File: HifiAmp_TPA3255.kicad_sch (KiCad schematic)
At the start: 129 parts, among them J1 PVDD 48V IN — NEEDS_DATA, J2 RCA L SE, J3 RCA R SE, J301 SPK_L, J302 SPK_R, J4 VOLUME_REMOTE, Q301 IPP330P10NM, Q302 IXTK200N10L2, U1 LM5010ASD, U2 LM2940IMP-12/NOPB, U3 TLV1117-33IDCY, U4 OPA1612AIDR, U5 OPA1612AIDR, U6 TPA3255B, U7 TPS3802K33DCKR, U8 LM5069-2

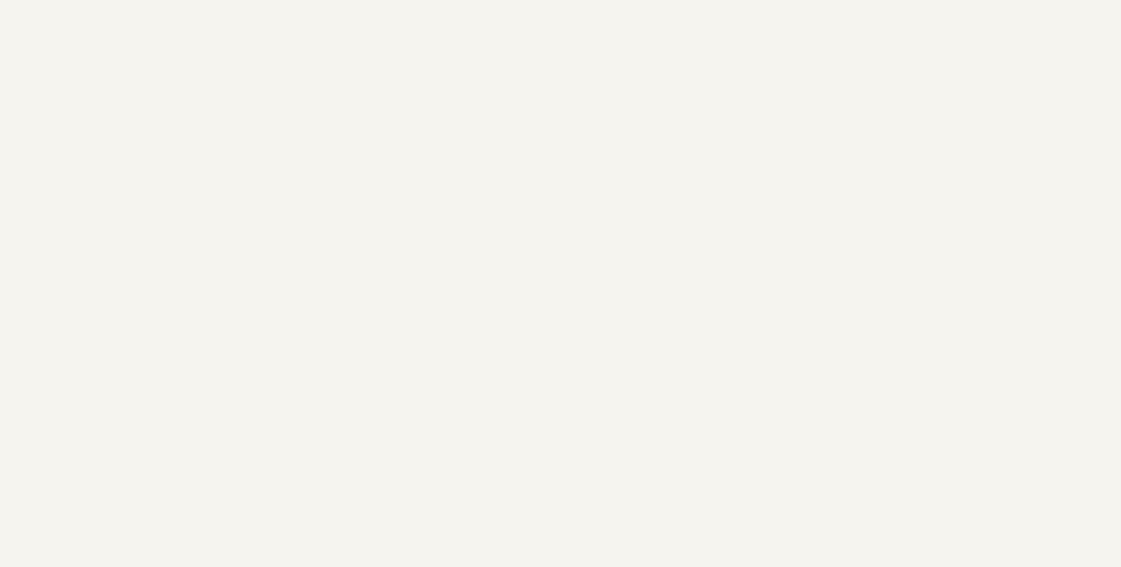
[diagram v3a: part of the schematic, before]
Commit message: feat(h1.4): add the TI Fig. 29 output RC networks (1 nF, 3.3 ohm + 10 nF) on OUT_A-D_F
Co-Authored-By: Claude Opus 5.5 <noreply@anthropic.com>
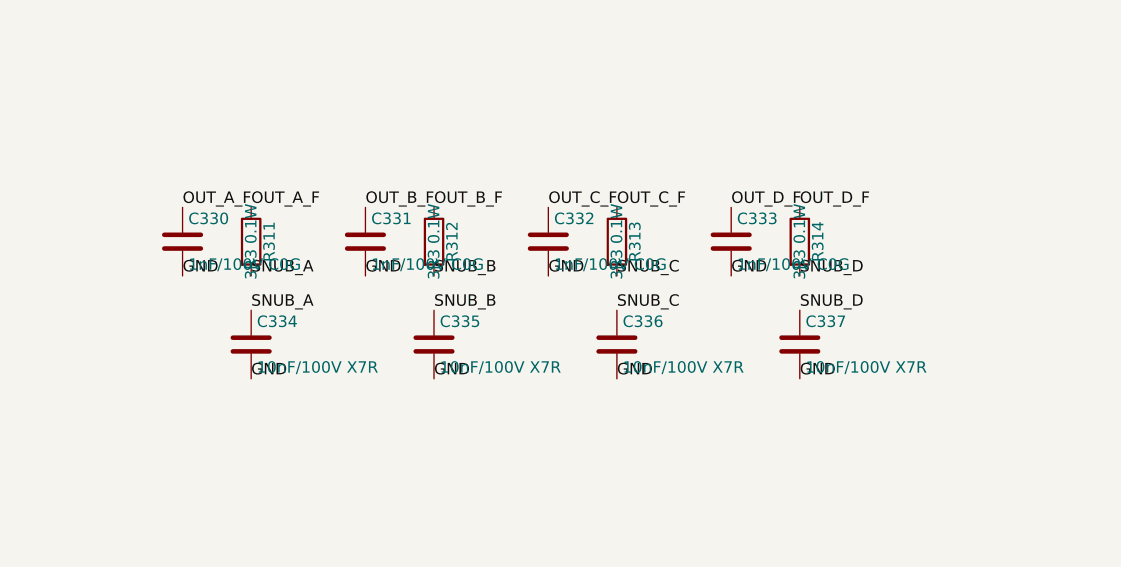
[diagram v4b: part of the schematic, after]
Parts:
- added C330, C331, C332, C333: 1nF/100V C0G, Capacitor_SMD:C_1206_3216Metric, symbol Device:C
- added C334, C335, C336, C337: 10nF/100V X7R, Capacitor_SMD:C_0603_1608Metric, symbol Device:C
- added R311, R312, R313, R314: 3R3 0.1W, Resistor_SMD:R_0603_1608Metric, symbol Device:R
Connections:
- net GND: now also C330.2, C331.2, C332.2, C333.2, C334.2, C335.2, C336.2, C337.2
- net OUT_A_F: now also C330.1, R311.1
- net OUT_B_F: now also C331.1, R312.1
- net OUT_C_F: now also C332.1, R313.1
- net OUT_D_F: now also C333.1, R314.1
- new net SNUB_A: C334.1, R311.2
- new net SNUB_B: C335.1, R312.2
- new net SNUB_C: C336.1, R313.2
- new net SNUB_D: C337.1, R314.2
